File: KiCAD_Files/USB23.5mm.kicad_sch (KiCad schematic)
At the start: 40 parts, among them J1 USB C Receptacle, J2 3.5mm Jack, U1 CM108B, U2 MAXIM MAX97220AETE+T

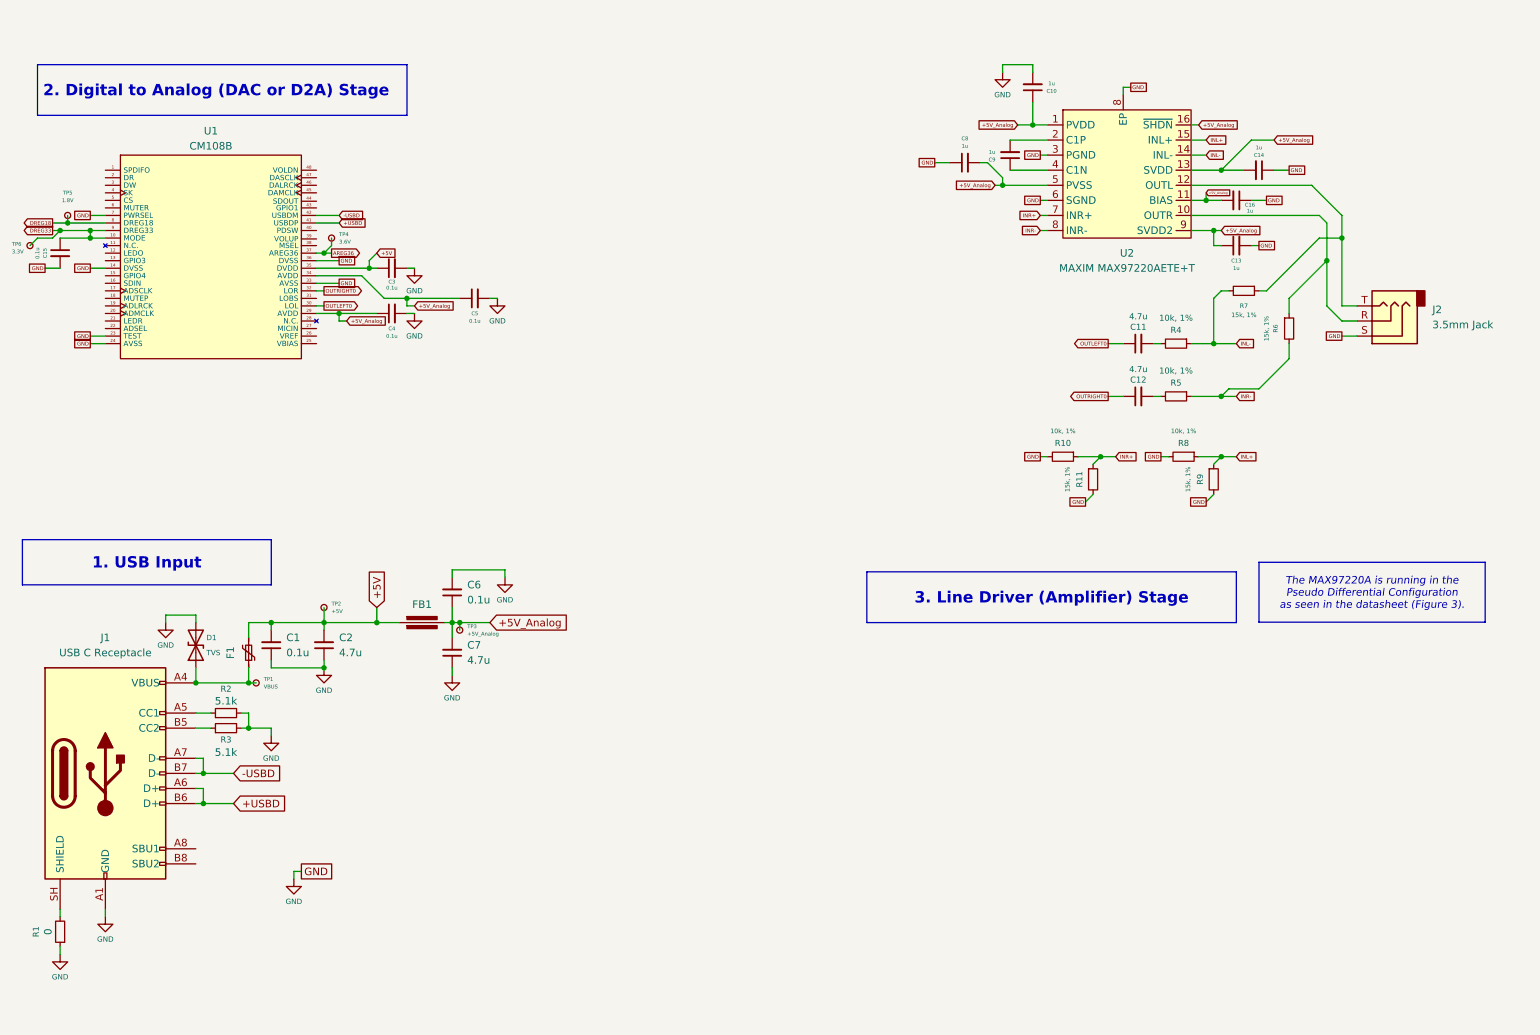
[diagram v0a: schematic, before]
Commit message: Revision A
Upload of First Revision of the board.
USB Signal integrity and output was revised.
PCB was designed, and gerber files have been plotted for production. JLCPCB BOM file is present dated 25/07/2026.
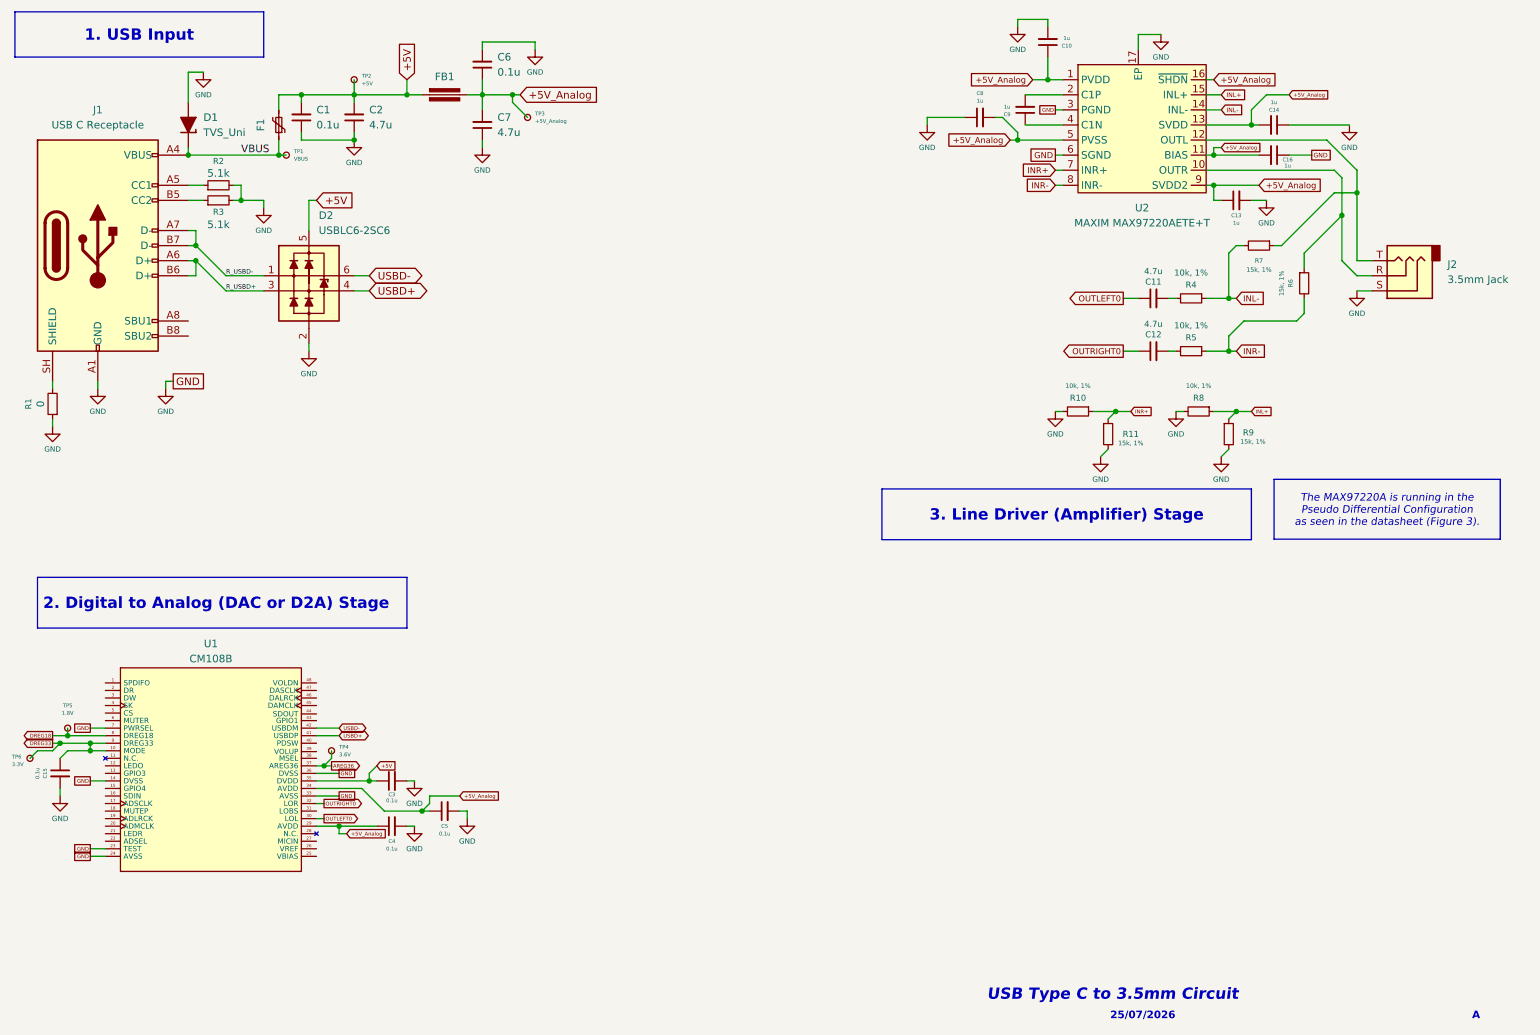
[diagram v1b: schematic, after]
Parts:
- removed D1: TVS, symbol Device:D_TVS
- added D1: TVS_Uni, PCM_Diode_SMD_Handsoldering_AKL:D_SOD-123F, symbol PCM_Diode_TVS_AKL:D_TVS_Unidirectional_Generic
- added D2: USBLC6-2SC6, PCM_Package_TO_SOT_SMD_AKL:SOT-23-6, symbol PCM_Diode_TVS_AKL:USBLC6-2SC6
- F1: footprint (none) -> Fuse:Fuse_2920_7451Metric_Pad2.10x5.45mm_HandSolder
- FB1: footprint (none) -> PCM_Ferrite_SMD_Handsoldering_AKL:Ferrite_0805_2012Metric
- J1: footprint (none) -> Connector_USB:USB_C_Receptacle_XKB_U262-16XN-4BVC11
- TP1, TP2, TP3, TP4, TP5, TP6: footprint (none) -> TestPoint:TestPoint_Pad_D1.5mm
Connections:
- net +5V: now also D2.5 (VP)
- net GND: now also U2.17 (EP), D1.2 (A), D2.2 (VN); no longer U2.8 (EP)
- net VBUS: now reaches F1.1, J1.A4 (VBUS), J1.A9 (VBUS), J1.B4 (VBUS), J1.B9 (VBUS), TP1.1
- net VBUS: now also D1.1 (K)
- net +USBD renamed R_USBD+
- net R_USBD+: now also D2.3 (L2); no longer U1.41 (USBDP)
- net -USBD renamed R_USBD-
- net R_USBD-: now also D2.1 (L1); no longer U1.42 (USBDM)
- new net USBD+: D2.4 (L2), U1.41 (USBDP)
- new net USBD-: D2.6 (L1), U1.42 (USBDM)
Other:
- note added: "25/07/2026"
- note added: "A"
- note added: "USB Type C to 3.5mm Circuit"
- moved on the sheet: C1, C10, C11, C12, C13, C14, C15, C16, C2, C3, C4, C5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
